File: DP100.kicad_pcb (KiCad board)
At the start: 2 copper layers, 36 x 46 mm, 63 parts, among them J1 SMA CONNECTOR, J2 Conn_01x06, J3 Conn_02x06_Odd_Even, Q1 2N7002, U1 NCP1117-3.3_SOT223, U2 Si5351A-B-GT, U3 AD9215BRUZ, Y1 25MHZ

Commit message: Se agregan notas en PCB
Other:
- board text added: "Minimo ancho de pista: 0,2mm Minimo diamtero via: 0,7 mm Minimo taladro: 0.4 mm Margen borde: 0,5 mm Grillas: 0.2mm 0.5mm 1mm"
- board text added: "Valores tomados en base a fabricante: Mayer PCB"
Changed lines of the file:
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@@
   (general
     (thickness 1.6)
-    (drawings 43)
+    (drawings 45)
     (tracks 379)
     (zones 0)
@@
     )
   )
+  (gr_text "Valores tomados en base a fabricante: Mayer PCB" (at 170.9 127.95) (layer Dwgs.User)
+    (effects (font (size 1 1) (thickness 0.15)))
+  )
+  (gr_text "Minimo ancho de pista: 0,2mm\nMinimo diamtero via: 0,7 mm\nMinimo taladro: 0.4 mm\nMargen borde: 0,5 mm\nGrillas:  0.2mm 0.5mm 1mm" (at 151.5 120.5) (layer Dwgs.User)
+    (effects (font (size 1 1) (thickness 0.15)) (justify left))
+  )
   (gr_text V1.0 (at 130.8 113) (layer B.SilkS)

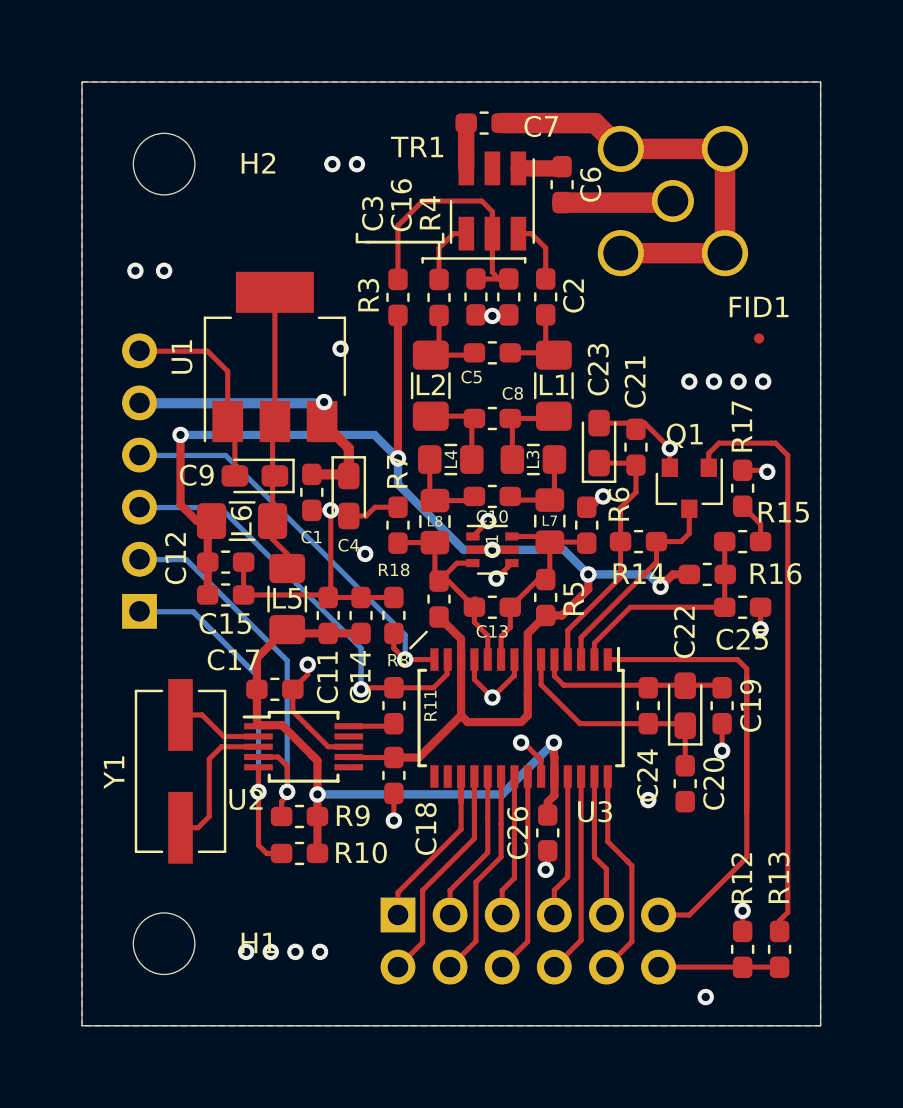
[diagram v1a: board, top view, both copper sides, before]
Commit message: Se realizan correcciones sugeridas el dia 20-4 -se agregan models 3d -se corrigen las notas -se modifican los planos de tierra segun sugerencia -se remueven serigrafias que se encontraban sobre vias -se remueve la via debajo de D1 -se alejan todas las vias de los pads de los componentes
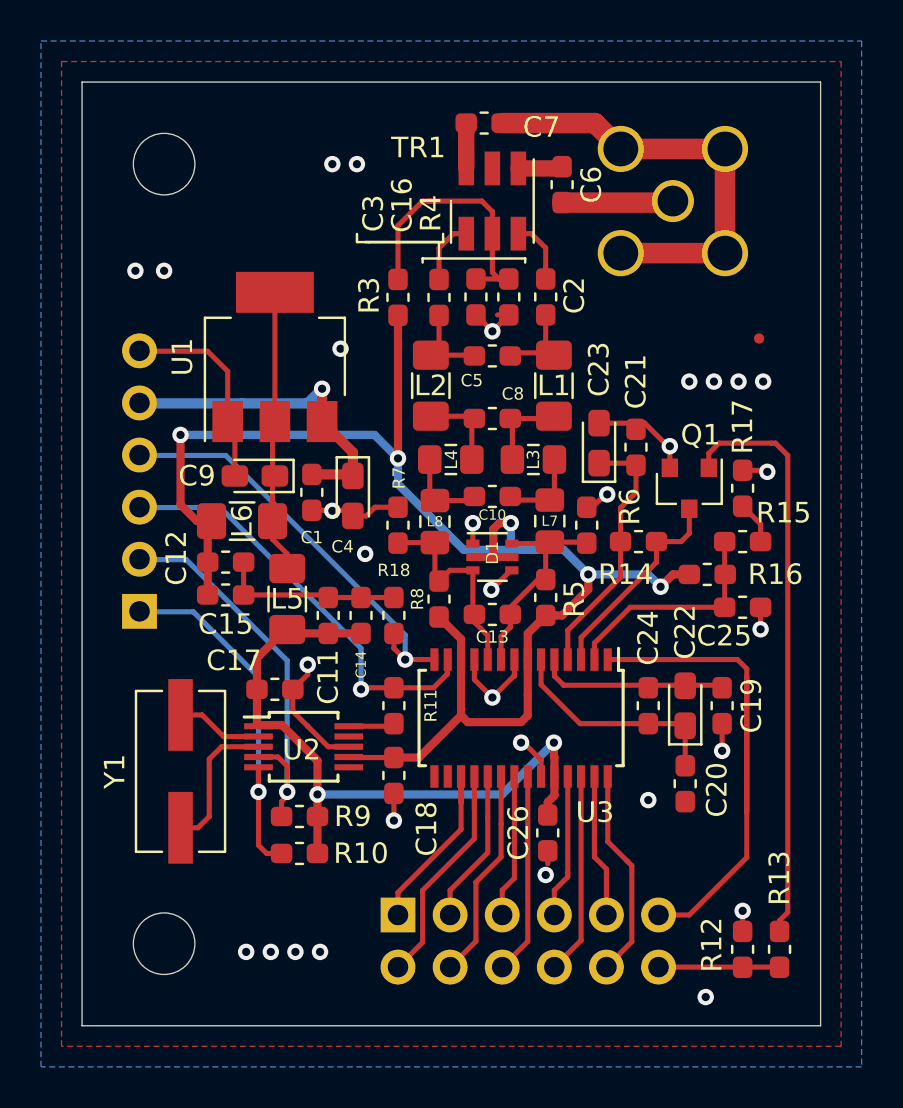
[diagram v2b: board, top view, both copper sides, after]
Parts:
- moved C13 0.35 mm to (129.0, 133.9)
- moved D1 0.35 mm to (129.0, 131.2)
- moved C4 0.20 mm to (122.2, 128.2)
- moved C5 0.15 mm to (129.0, 121.3)
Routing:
- net +3.3VA: track 70.6 -> 74.2 mm
- net GND: track 57.9 -> 54.6 mm
- net +5V: track 14.6 -> 16.5 mm
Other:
- board text added: "Minimo ancho de pista: 0,25mm Minimo diamtero via: 0,8 mm Minimo taladro: 0.4 mm Margen borde: 0,5 mm Clearance minimo: 0,2mm Grillas: 0.2mm 0.5mm 1mm Terminacion: HASL"
- board text removed: "Minimo ancho de pista: 0,2mm Minimo diamtero via: 0,7 mm Minimo taladro: 0.4 mm Margen borde: 0,5 mm Grillas: 0.2mm 0.5mm 1mm"
